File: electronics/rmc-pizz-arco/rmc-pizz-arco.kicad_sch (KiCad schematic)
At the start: 117 parts, among them J1 PZT, J2 PZT, J3 PZT, J4 PZT, J5 PZT, J6 PZT, J7 DIN-8, J8 PIZZ/ARCO, J9 12V DC, U1 OPA2191, U2 OPA2191, U3 OPA2191, U4 OPA2191, U5 OPA2191, U6 OPA2191, U7 OPA2191, U8 CD4066B, U9 CD4066B

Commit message: Fixed errors and wrote up pcbway order
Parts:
- removed C901, C902: 100n, Capacitor_SMD:C_0805_2012Metric, symbol Device:C
- added C803, C804, C805, C806: 100n, Capacitor_SMD:C_0805_2012Metric, symbol Device:C
- added U10: CD4066B, Package_SO:SO-14_3.9x8.65mm_P1.27mm, symbol Analog_Switch:CD4066BM
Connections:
- net AGND: now also U8.10, U8.8, C803.2, C804.2, C805.2, C806.2, U10.10, U10.11, U10.2, U10.4, U10.8, U10.9
- net SWN3: now also U9.1; no longer U8.8
- net SWN4: now also U9.3; no longer U8.10
- net SWN5: now also U10.1; no longer U9.1
- net SWN6: now also U10.3; no longer U9.3
- net SW_CTL: now also U10.13, U10.5; no longer U8.12, U8.6
- net V+: now also C803.1, C805.1, U10.14 (V_{DD})
- net V-: now also U8.12, U8.6, C804.1, C806.1, U10.12, U10.6, U10.7 (V_{SS})
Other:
- moved on the sheet: U9A, U9B, U9C, U9D, U9E

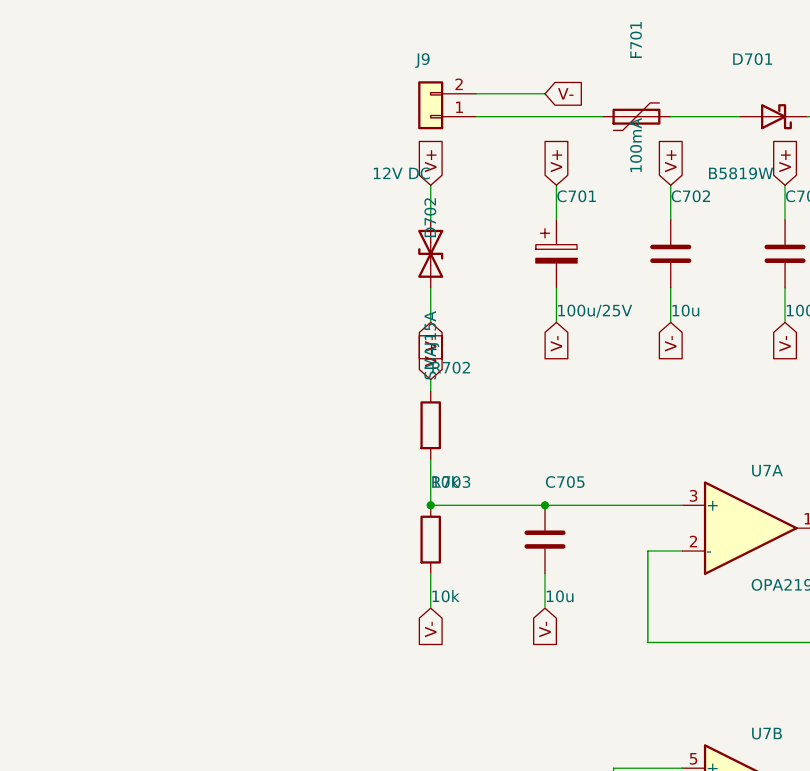
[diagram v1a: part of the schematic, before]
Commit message: We believe this system can be safely run at 9v DC. We now check for KiCad installation and fail if not found. We updated docs on what happens if the power supply fails.
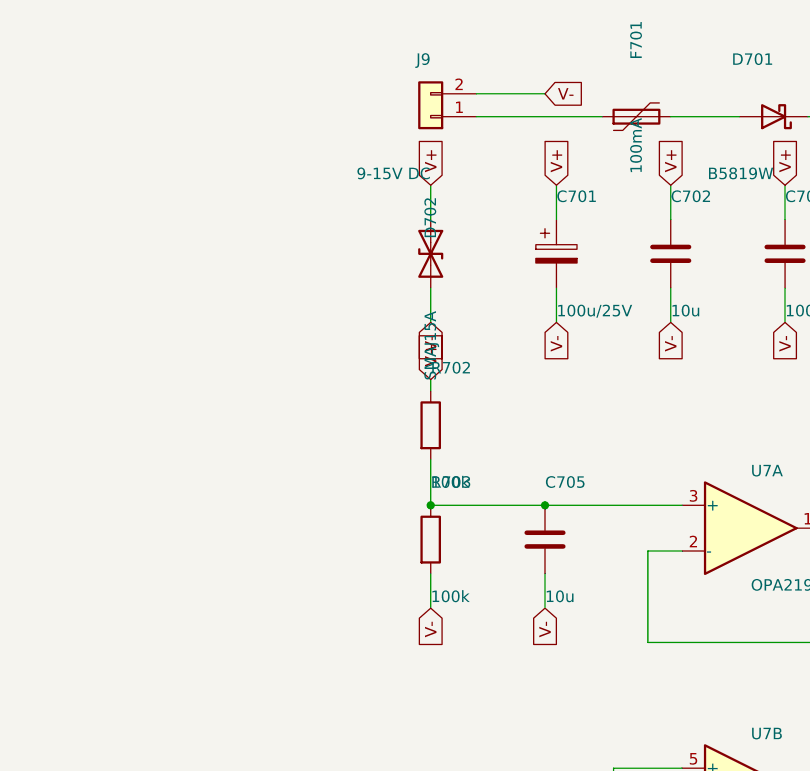
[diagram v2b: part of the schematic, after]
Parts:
- J9: value 12V DC -> 9-15V DC
- R702, R703: value 10k -> 100k
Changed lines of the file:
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@@
 			)
 		)
-		(property "Value" "12V DC"
+		(property "Value" "9-15V DC"
 			(at 299.72 46.99 0)
 			(effects
@@
 			)
 		)
-		(property "Value" "10k"
+		(property "Value" "100k"
 			(at 299.72 81.28 0)
 			(effects
@@
 			)
 		)
-		(property "Value" "10k"
+		(property "Value" "100k"
 			(at 299.72 93.98 0)
 			(effects

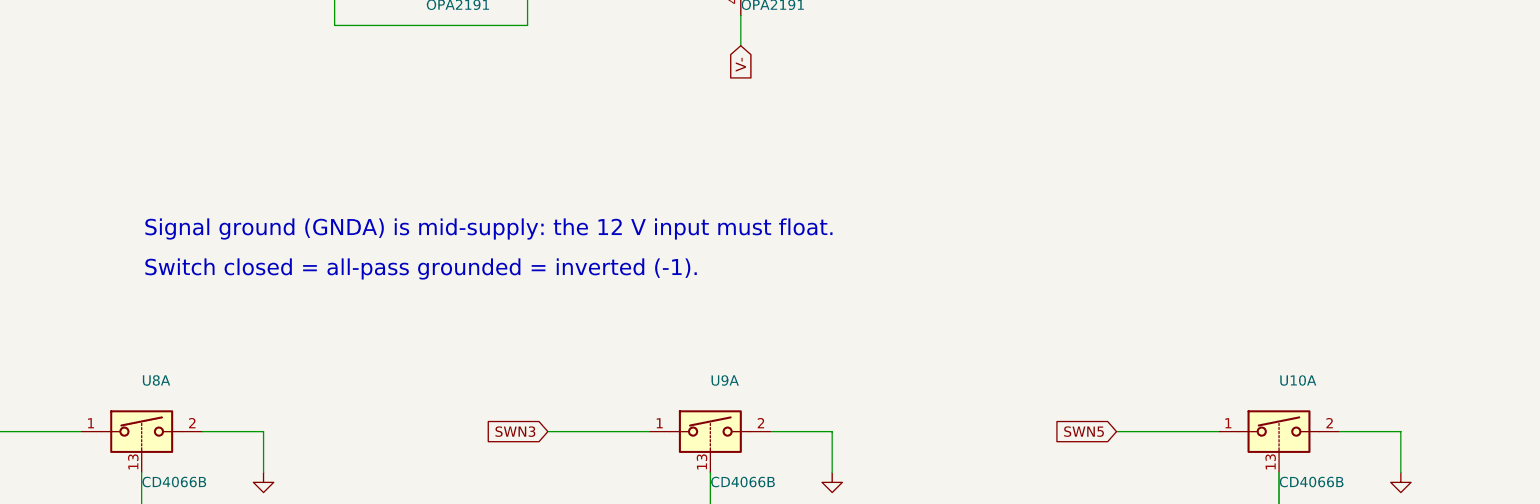
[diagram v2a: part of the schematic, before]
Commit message: Made it clear that we believe this system can run on 9v
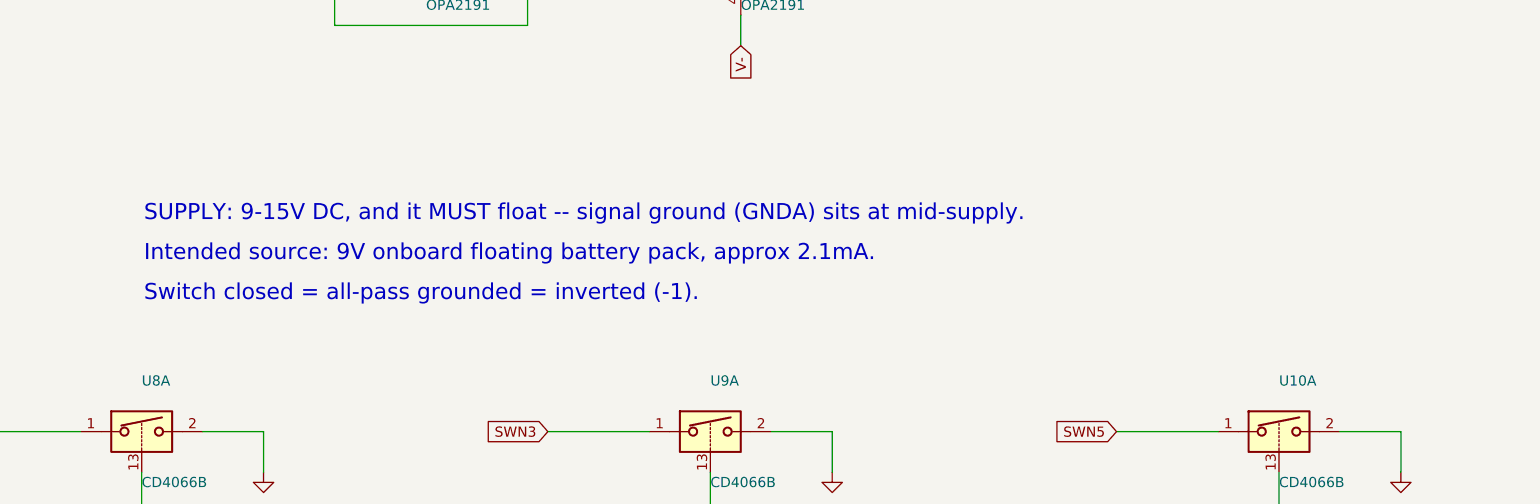
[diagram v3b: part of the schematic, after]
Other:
- note added: "Intended source: 9V onboard floating battery pack, approx 2.1mA."
- note added: "SUPPLY: 9-15V DC, and it MUST float -- signal ground (GNDA) sits at mid-supply."
- note removed: "Signal ground (GNDA) is mid-supply: the 12 V input must float."
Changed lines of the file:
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@@
 		)
 	)
-	(text "Signal ground (GNDA) is mid-supply: the 12 V input must float."
-		(at 300 150 0)
+	(text "SUPPLY: 9-15V DC, and it MUST float -- signal ground (GNDA) sits at mid-supply."
+		(at 300 148 0)
+		(effects
+			(font
+				(size 2 2)
+			)
+			(justify left)
+		)
+	)
+	(text "Intended source: 9V onboard floating battery pack, approx 2.1mA."
+		(at 300 153 0)
 		(effects
 			(font
@@
 	)
 	(text "Switch closed = all-pass grounded = inverted (-1)."
-		(at 300 155 0)
+		(at 300 158 0)
 		(effects
 			(font

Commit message: First pass at reworking board now we know that power will be provided by a modified poly-drive ii via pins 7 and 8
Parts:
- removed C105, C205, C305, C405, C505, C605: 1n5, Capacitor_SMD:C_0805_2012Metric, symbol Device:C
- removed C106, C107, C206, C207, C306, C307, C406, C407, C506, C507, C606, C607, C703, C704, C708, C709, C801, C802, C803, C804, C805, C806: 100n, Capacitor_SMD:C_0805_2012Metric, symbol Device:C
- removed C702, C705, C706, C707: 10u, Capacitor_SMD:C_0805_2012Metric, symbol Device:C
- removed D701: B5819W, Diode_SMD:D_SOD-123, symbol Device:D_Schottky
- removed D702: SMAJ15A, Diode_SMD:D_SMA, symbol Device:D_TVS
- removed F701: 100mA, Fuse:Fuse_1206_3216Metric, symbol Device:Polyfuse
- removed J9: 9-15V DC, Connector_PinHeader_2.54mm:PinHeader_1x02_P2.54mm_Vertical, symbol Connector_Generic:Conn_01x02
- removed JP1: DNP, Jumper:SolderJumper-2_P1.3mm_Open_Pad1.0x1.5mm, symbol Jumper:SolderJumper_2_Open
- removed R703: 100k, Resistor_SMD:R_0805_2012Metric, symbol Device:R
- removed R704: 10R, Resistor_SMD:R_0805_2012Metric, symbol Device:R
- removed U10, U8, U9: CD4066B, Package_SO:SO-14_3.9x8.65mm_P1.27mm, symbol Analog_Switch:CD4066BM
- removed U6, U7: OPA2191, Package_SO:SOIC-8_3.9x4.9mm_P1.27mm, symbol rmc:OPA2191
- added C901, C902, C903, C904: 4u7/25V, Capacitor_SMD:C_1206_3216Metric, symbol Device:C
- added unit 5 of U1
- added unit 4 of U1
- added unit 4 of U2
- added unit 5 of U2
- added unit 4 of U3
- added unit 5 of U3
- added unit 4 of U4
- added unit 5 of U4
- added unit 4 of U5
- added unit 5 of U5
- C101, C102, C103, C201, C202, C203, C301, C302, C303, C401, C402, C403, C501, C502, C503, C601, C602, C603: footprint Capacitor_SMD:C_0805_2012Metric -> Capacitor_SMD:C_1206_3216Metric
- C104, C204, C304, C404, C504, C604: value 220p -> 1n8 C0G; footprint Capacitor_SMD:C_0805_2012Metric -> Capacitor_SMD:C_1206_3216Metric
- C701: value 100u/25V -> 10n; footprint Capacitor_SMD:CP_Elec_6.3x5.4 -> Capacitor_SMD:C_1206_3216Metric; symbol Device:C_Polarized -> Device:C
- J7: footprint Connector_PinHeader_2.54mm:PinHeader_1x08_P2.54mm_Vertical -> Connector_PinHeader_2.54mm:PinHeader_1x09_P2.54mm_Vertical; symbol Connector_Generic:Conn_01x08 -> Connector_Generic:Conn_01x09
- R101, R102, R103, R201, R202, R203, R301, R302, R303, R401, R402, R403, R501, R502, R503, R601, R602, R603: footprint Resistor_SMD:R_0805_2012Metric -> Resistor_SMD:R_1206_3216Metric
- R104, R105, R106, R204, R205, R206, R304, R305, R306, R404, R405, R406, R504, R505, R506, R604, R605, R606: value 47k -> 47k 1%; footprint Resistor_SMD:R_0805_2012Metric -> Resistor_SMD:R_1206_3216Metric
- R701: value 100k -> 1M; footprint Resistor_SMD:R_0805_2012Metric -> Resistor_SMD:R_1206_3216Metric
- R702: value 100k -> 20k; footprint Resistor_SMD:R_0805_2012Metric -> Resistor_SMD:R_1206_3216Metric
- U1, U2, U3: value OPA2191 -> OPA4191; footprint Package_SO:SOIC-8_3.9x4.9mm_P1.27mm -> Package_SO:SOIC-14_3.9x8.7mm_P1.27mm; symbol rmc:OPA2191 -> rmc:OPA4191
- U4, U5: value OPA2191 -> CD4066B; footprint Package_SO:SOIC-8_3.9x4.9mm_P1.27mm -> Package_SO:SO-14_3.9x8.65mm_P1.27mm; symbol rmc:OPA2191 -> Analog_Switch:CD4066BM
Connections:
- net AGND: now also C701.2, J7.9 (Pin_9), U4.2, U4.4, U4.9, U5.2, U5.4, U5.9, C901.2, C902.2, C903.2, C904.2, U4.10, U4.11, U5.10, U5.11; no longer J7.7 (Pin_7)
- net SWN1: now also U4.1, U1.12 (+); no longer U1.5 (+)
- net SWN2: now also U1.10 (+), U4.3; no longer U2.5 (+)
- net SWN3: now also U4.8, U2.12 (+); no longer U3.5 (+)
- net SWN4: now also U2.10 (+), U5.1; no longer U4.5 (+)
- net SWN5: now also U5.3, U3.12 (+); no longer U5.5 (+)
- net SWN6: now also U3.10 (+), U5.8
- net SW_CTL: now also C701.1, J8.2 (Pin_2), U4.13, U4.5, U4.6, U5.13, U5.5, U5.6; no longer J8.1 (Pin_1)
- net V+: now also J7.7 (Pin_7), C901.1, C903.1, U1.4 (V+), U2.4 (V+), U3.4 (V+), U4.14 (V_{DD}), U5.14 (V_{DD}); no longer C701.1, J8.2 (Pin_2), U1.8 (V+), U2.8 (V+), U3.8 (V+), U4.8 (V+), U5.8 (V+)
- net V-: now also J7.8 (Pin_8), C902.1, C904.1, U1.11 (V-), U2.11 (V-), U3.11 (V-), U4.12, U4.7 (V_{SS}), U5.12, U5.7 (V_{SS}); no longer C701.2, U1.4 (V-), U2.4 (V-), U3.4 (V-), U4.4 (V-), U5.4 (V-)
- net at C402.2, C404.1, R406.2: now also U2.8; no longer U4.7
- net at C601.1, R601.2: now also U3.5 (+)
- net SW_TOG: now reaches R702.2
- net SW_TOG: now also J8.1 (Pin_1)
- net at C302.1, R304.2, R306.1: now also U2.13 (-); no longer U3.6 (-)
- net at C302.2, C304.1, R306.2: now also U2.14; no longer U3.7
- net at R603.2, R604.1, R605.1: now also U3.7
- net at C602.1, R604.2, R606.1: now also U3.9 (-)
- net at C202.2, C204.1, R206.2: now also U1.8; no longer U2.7
- net at C402.1, R404.2, R406.1: now also U2.9 (-); no longer U4.6 (-)
- net at C501.1, R501.2: now also U3.3 (+); no longer U5.3 (+)
- net at C102.2, C104.1, R106.2: now also U1.14; no longer U1.7
- net at C301.1, R301.2: now also U2.3 (+); no longer U3.3 (+)
- net at R303.2, R304.1, R305.1: now also U2.1; no longer U3.1
- net at R203.2, R204.1, R205.1: now also U1.7; no longer U2.1
- net at C202.1, R204.2, R206.1: now also U1.9 (-); no longer U2.6 (-)
- net at R303.1: now also U2.2 (-); no longer U3.2 (-)
- net at R503.1: now also U3.2 (-); no longer U5.2 (-)
- net at R503.2, R504.1, R505.1: now also U3.1; no longer U5.1
- net at C602.2, C604.1, R606.2: now also U3.8
- net at C502.1, R504.2, R506.1: now also U3.13 (-); no longer U5.6 (-)
- net at C502.2, C504.1, R506.2: now also U3.14; no longer U5.7
- net at R403.2, R404.1, R405.1: now also U2.7; no longer U4.1
- net at R603.1: now also U3.6 (-)
- net at R403.1: now also U2.6 (-); no longer U4.2 (-)
- net at C201.1, R201.2: now also U1.5 (+); no longer U2.3 (+)
- net at C102.1, R104.2, R106.1: now also U1.13 (-); no longer U1.6 (-)
- net at C401.1, R401.2: now also U2.5 (+); no longer U4.3 (+)
- net at R203.1: now also U1.6 (-); no longer U2.2 (-)
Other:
- note added: "DIN-8 pin 7 = +4.5V, pin 8 = -4.5V, shell = ground; approx 2mA, drawn symmetrically."
- note added: "Drains must stay symmetrical: no DC path from either rail to AGND anywhere."
- note added: "SUPPLY: +/-4.5V from Poly-Drive II. Ground is the DIN shell -- the board has no supply of its own."
- note added: "Switch CLOSED = all-pass inverted = elements in phase = PIZZ. Open = ARCO."
- note removed: "Intended source: 9V onboard floating battery pack, approx 2.1mA."
- note removed: "SUPPLY: 9-15V DC, and it MUST float -- signal ground (GNDA) sits at mid-supply."
- note removed: "Switch closed = all-pass grounded = inverted (-1)."
- moved on the sheet: C301, C302, C303, C304, C401, C402, C403, C404, C501, C502, C503, C504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
